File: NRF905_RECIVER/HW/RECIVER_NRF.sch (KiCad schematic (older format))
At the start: 0 parts

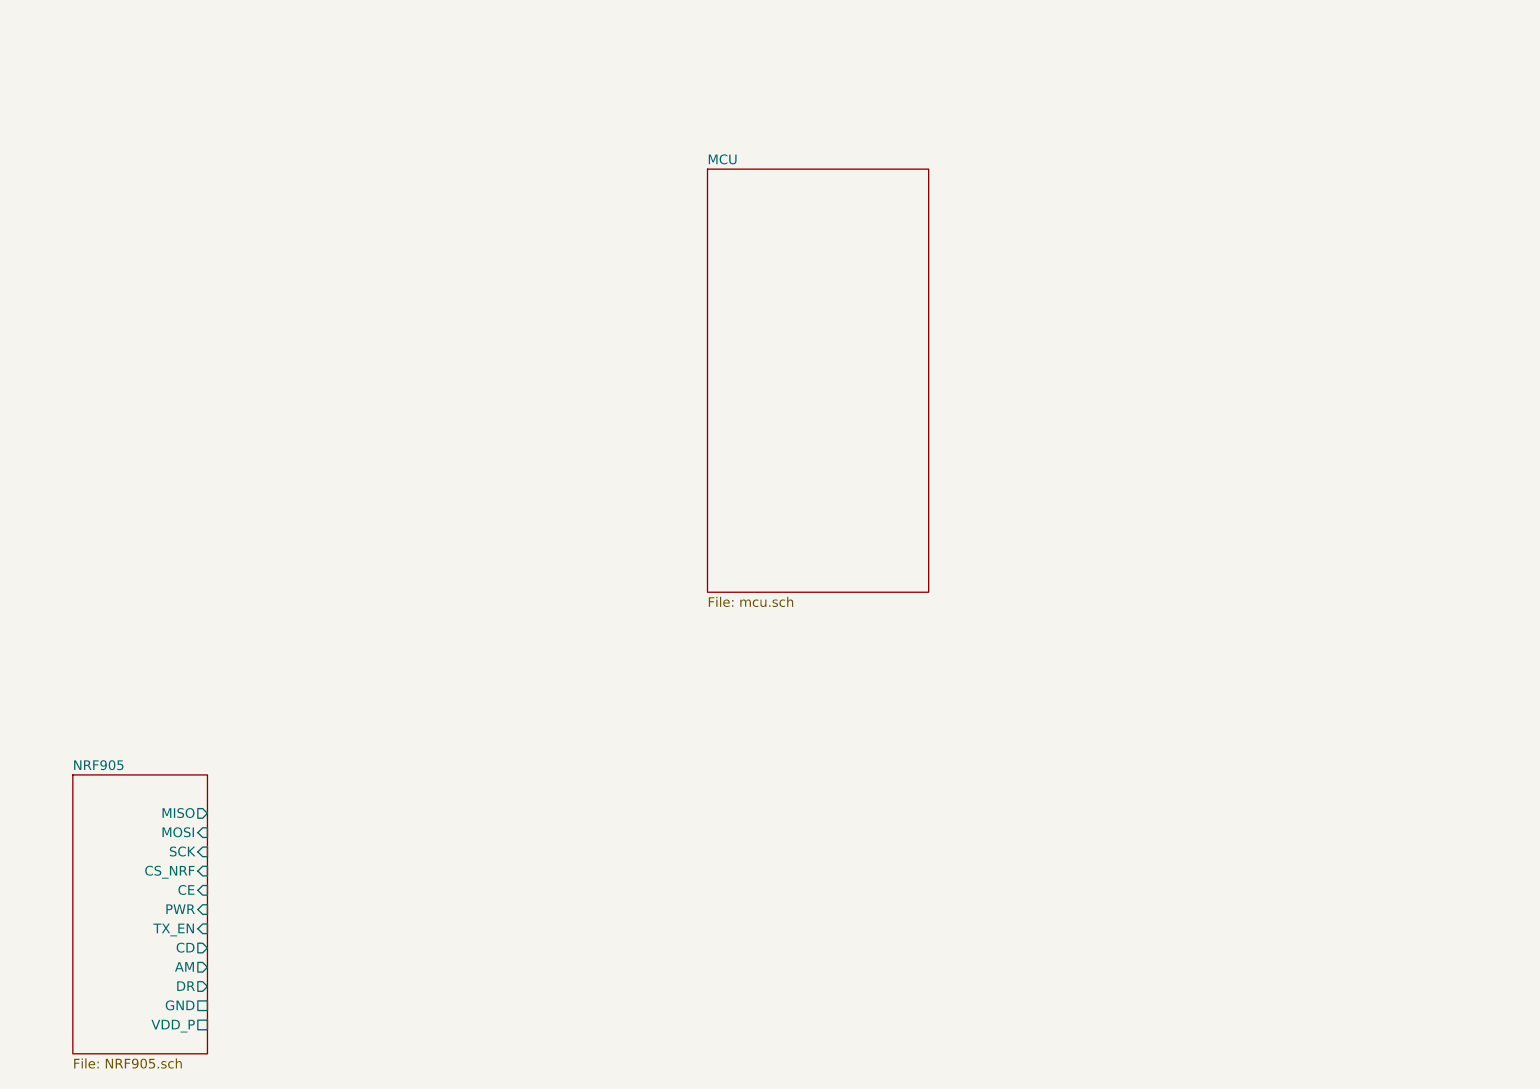
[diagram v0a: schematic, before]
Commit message: Изменение в схемотехнике приемника. Добавлен TFT модуль, WIFI модуль.
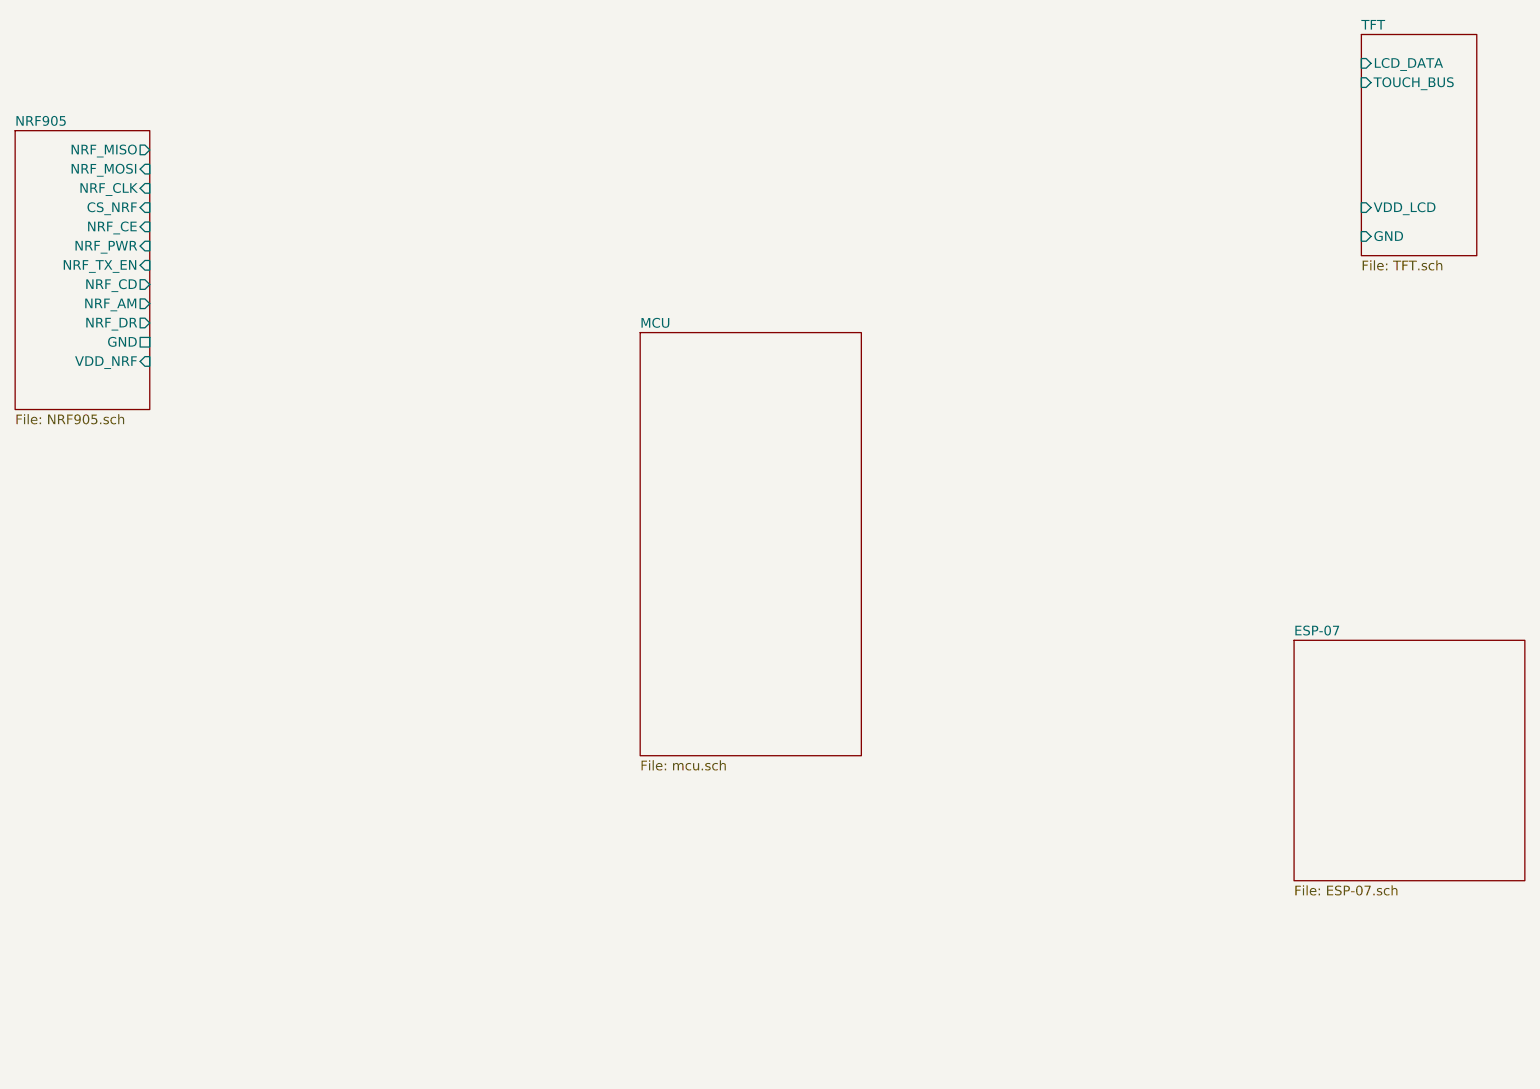
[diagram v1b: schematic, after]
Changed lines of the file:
@@
 $Descr A4 11693 8268
 encoding utf-8
-Sheet 1 3
+Sheet 1 5
 Title ""
 Date ""
@@
 $EndDescr
 $Sheet
-S 5100 1600 1150 2200
+S 4750 2450 1150 2200
 U 5F662B70
 F0 "MCU" 50
@@
 $EndSheet
 $Sheet
-S 1800 4750 700  1450
+S 8500 900  600  1150
+U 5F661468
+F0 "TFT" 50
+F1 "TFT.sch" 50
+F2 "LCD_DATA" I L 8500 1050 50
+F3 "GND" I L 8500 1950 50
+F4 "VDD_LCD" I L 8500 1800 50
+F5 "TOUCH_BUS" I L 8500 1150 50
+$EndSheet
+$Sheet
+S 8150 4050 1200 1250
+U 5F662950
+F0 "ESP-07" 50
+F1 "ESP-07.sch" 50
+$EndSheet
+$Sheet
+S 1500 1400 700  1450
 U 5F6650A9
 F0 "NRF905" 50
 F1 "NRF905.sch" 50
-F2 "MISO" O R 2500 4950 50
-F3 "MOSI" I R 2500 5050 50
-F4 "SCK" I R 2500 5150 50
-F5 "CS_NRF" I R 2500 5250 50
-F6 "CE" I R 2500 5350 50
-F7 "PWR" I R 2500 5450 50
-F8 "TX_EN" I R 2500 5550 50
-F9 "CD" O R 2500 5650 50
-F10 "AM" O R 2500 5750 50
-F11 "DR" O R 2500 5850 50
-F12 "GND" U R 2500 5950 50
-F13 "VDD_P" U R 2500 6050 50
+F2 "NRF_MISO" O R 2200 1500 50
+F3 "NRF_MOSI" I R 2200 1600 50
+F4 "NRF_CLK" I R 2200 1700 50
+F5 "CS_NRF" I R 2200 1800 50
+F6 "NRF_CE" I R 2200 1900 50
+F7 "NRF_PWR" I R 2200 2000 50
+F8 "NRF_TX_EN" I R 2200 2100 50
+F9 "NRF_CD" O R 2200 2200 50
+F10 "NRF_AM" O R 2200 2300 50
+F11 "NRF_DR" O R 2200 2400 50
+F12 "GND" U R 2200 2500 50
+F13 "VDD_NRF" I R 2200 2600 50
 $EndSheet
 $EndSCHEMATC

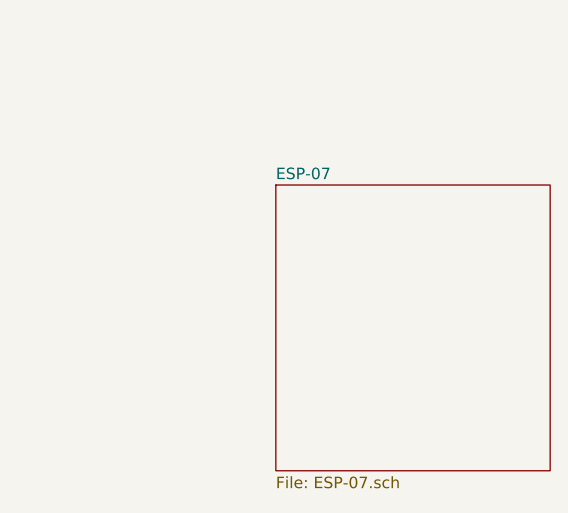
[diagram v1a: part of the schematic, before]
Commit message: Изменена структура проека. Добавлен шаблон проекта для ESP32. Изменение в схемотехнике WIFI модуль с ESP-07 изменени на ESP32 WROVER-IB
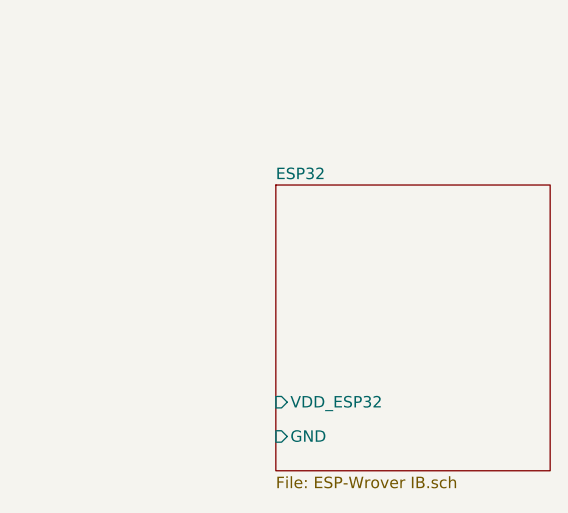
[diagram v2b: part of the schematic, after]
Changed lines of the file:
@@
 S 8150 4050 1200 1250
 U 5F662950
-F0 "ESP-07" 50
-F1 "ESP-07.sch" 50
+F0 "ESP32" 50
+F1 "ESP-Wrover IB.sch" 50
+F2 "GND" I L 8150 5150 50
+F3 "VDD_ESP32" I L 8150 5000 50
 $EndSheet
 $Sheet
